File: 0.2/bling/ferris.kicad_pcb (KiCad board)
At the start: 2 copper layers, 208.8 x 89.8 mm, 145 parts, among them J1 TYPE-C-31-M-12, K0_0 KEYSW, K0_1 KEYSW, K0_2 KEYSW, K0_3 KEYSW, K0_4 KEYSW, K0_5 KEYSW, K0_6 KEYSW, K0_7 KEYSW, K0_8 KEYSW, K0_9 KEYSW, K1_0 KEYSW, K1_1 KEYSW, K1_2 KEYSW, K1_3 KEYSW, K1_4 KEYSW, K1_5 KEYSW, K1_6 KEYSW, K1_7 KEYSW, K1_8 KEYSW, K1_9 KEYSW, K2_0 KEYSW, K2_1 KEYSW, K2_2 KEYSW, K2_3 KEYSW, K2_4 KEYSW, K2_5 KEYSW, K2_6 KEYSW, K2_7 KEYSW, K2_8 KEYSW, K2_9 KEYSW, K3_3 KEYSW, K3_4 KEYSW, K3_5 KEYSW, K3_6 KEYSW, Q1 PDTC123JT,215, SW1 B3U-1000P, U1 STM32F072CBT6, U2 MCP23017-E/SO, U3 MCP1700T-3302E/TT, U4 SRV05-4, U5 IS31FL3731, U6 IS31FL3731

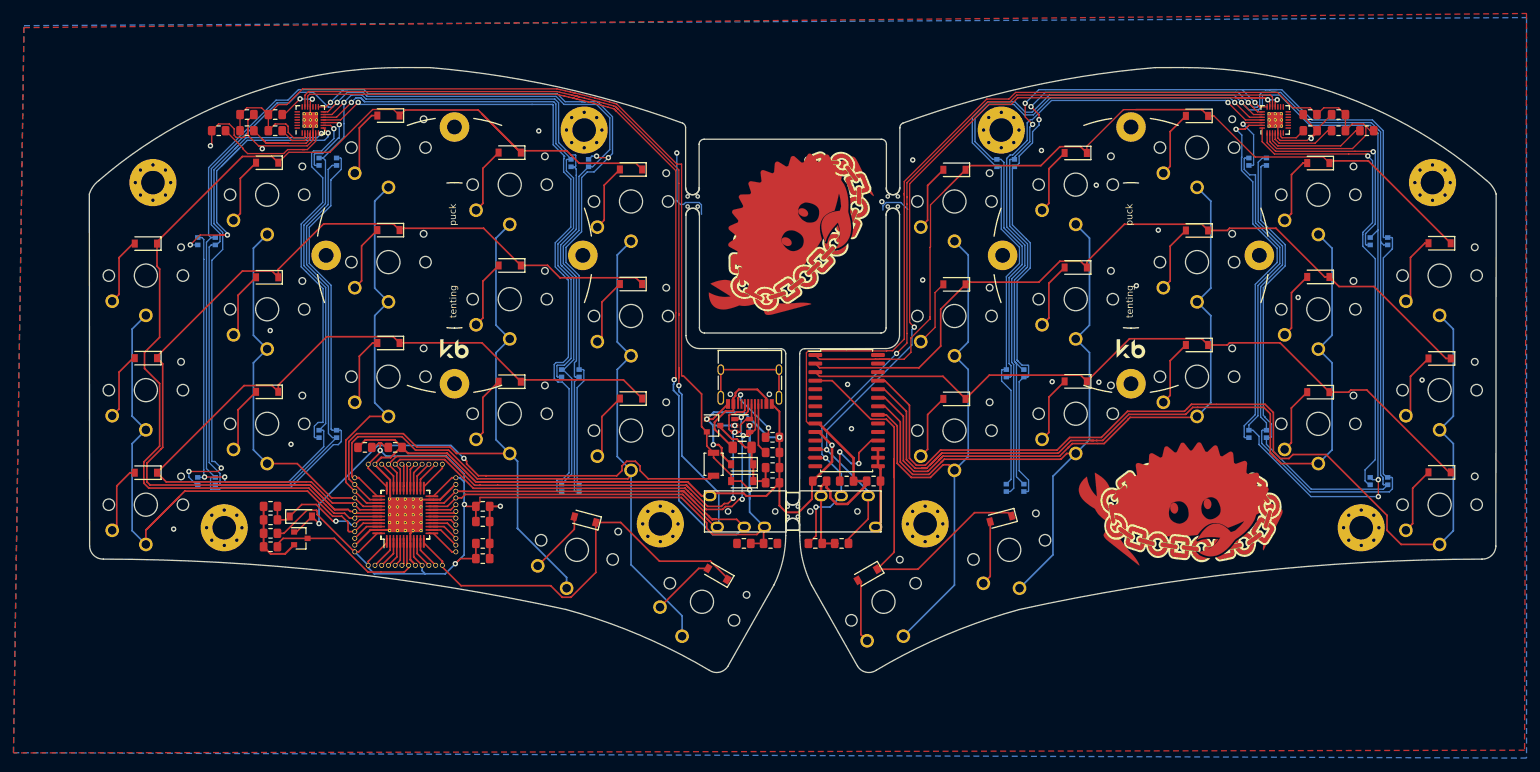
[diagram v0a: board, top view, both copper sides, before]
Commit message: Update to KiCad 7.0
... and prune outdated project files (need to check)
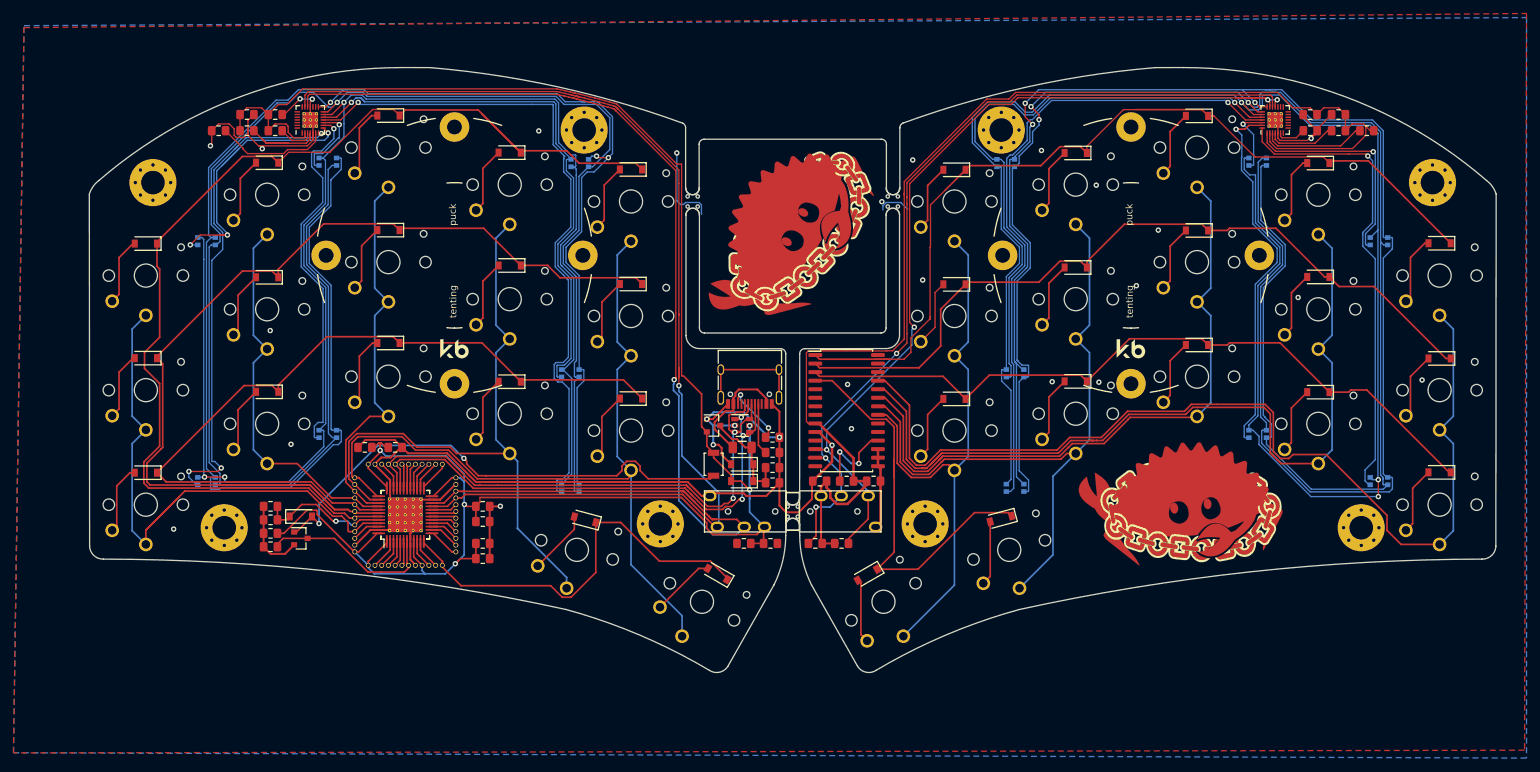
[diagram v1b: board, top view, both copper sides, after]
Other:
- net class Default removed
- net class Power removed
